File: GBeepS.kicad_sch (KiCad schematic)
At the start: 35 parts, among them J1 Ant, U1 NCP160xMX, U2 MMC3416xPJ, U3 ZOE-M8Q

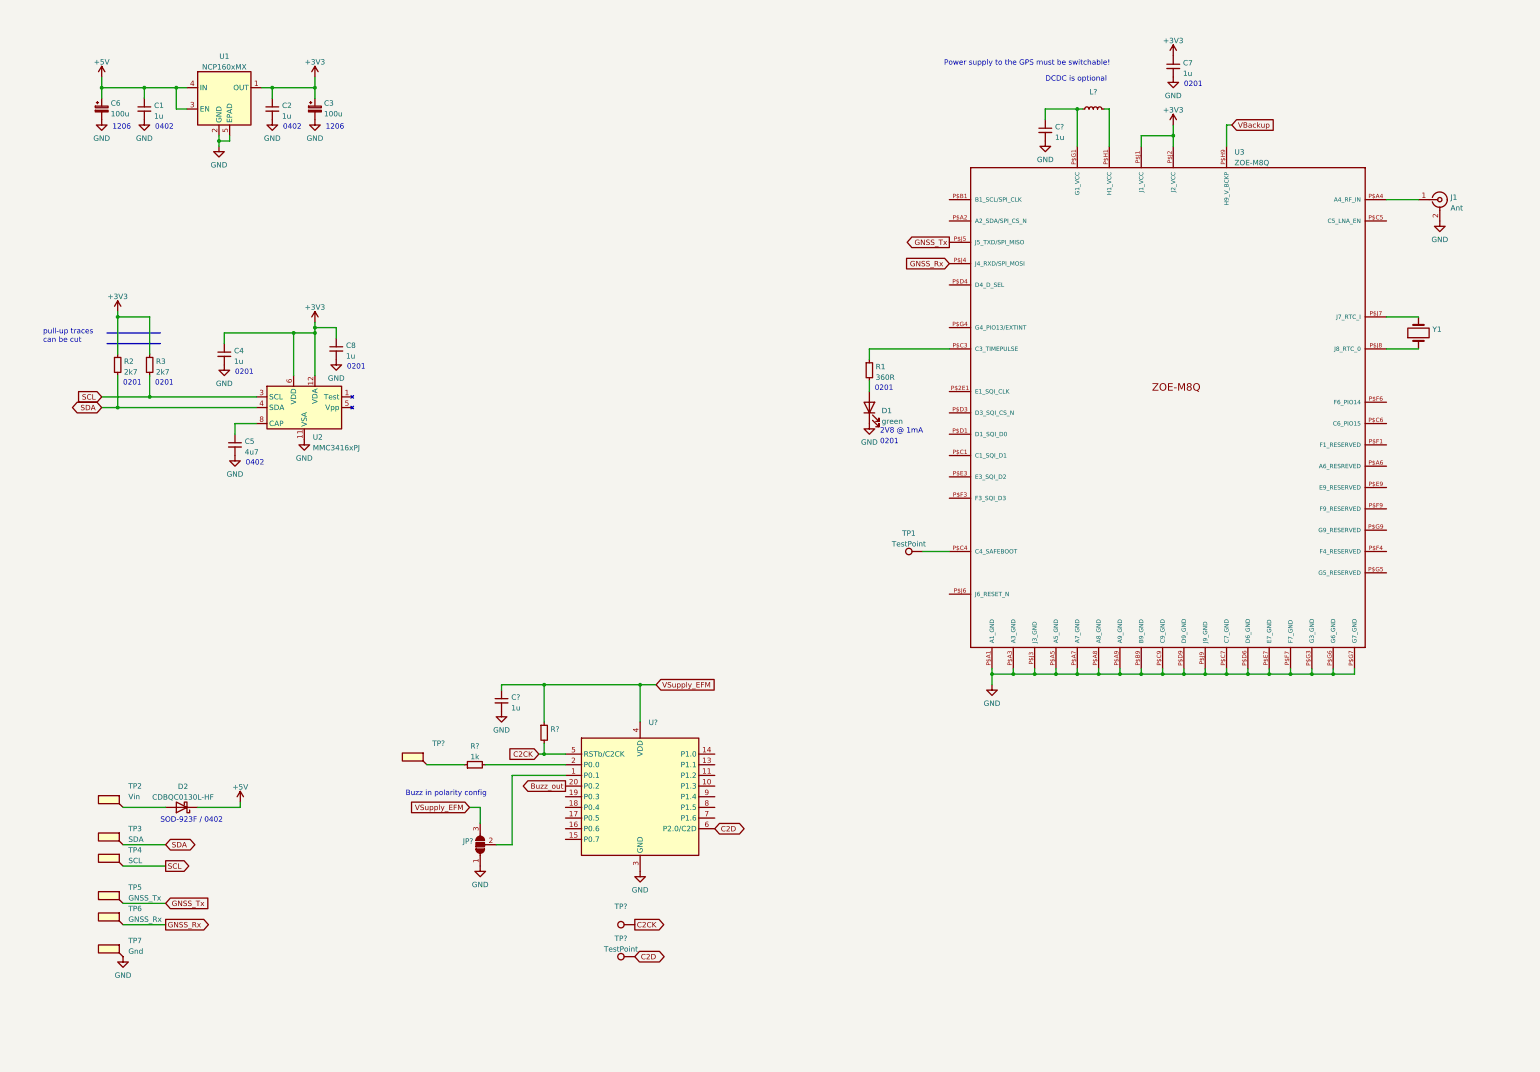
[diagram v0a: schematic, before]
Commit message: update schematic
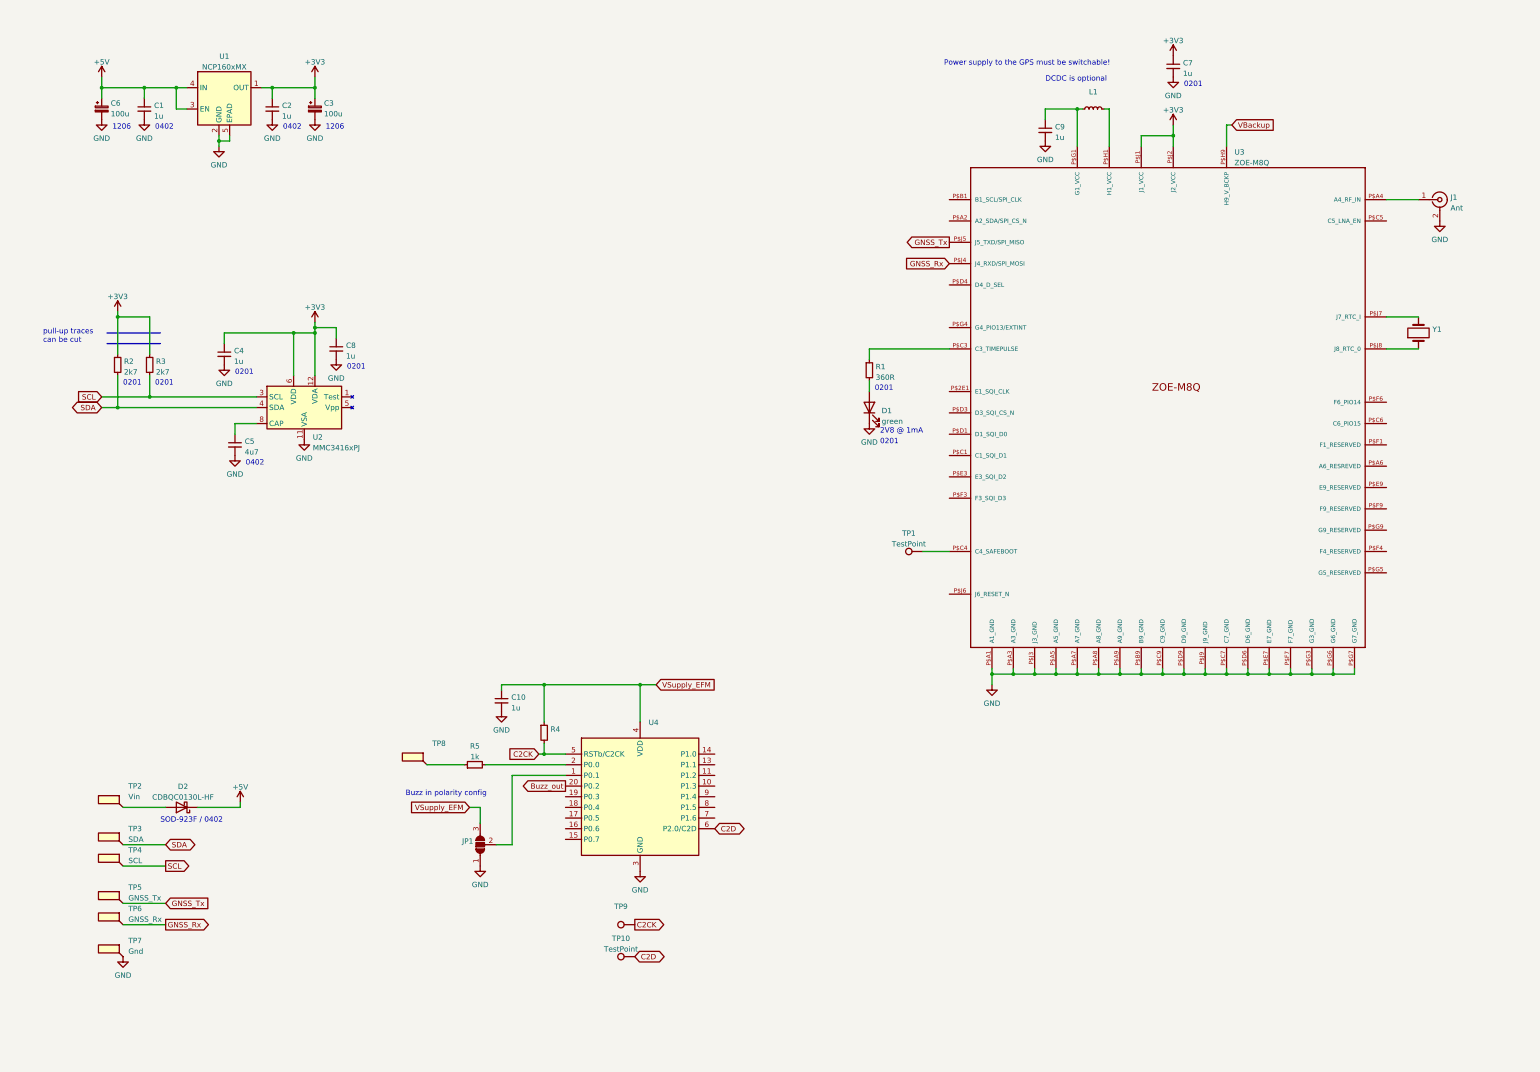
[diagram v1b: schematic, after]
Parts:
- gave numbers to parts that had none: 10
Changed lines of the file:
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@@
   (symbol (lib_id "MCU_SiliconLabs:EFM8BB10F8G-A-QFN20") (at 161.29 204.47 0) (unit 1)
     (in_bom yes) (on_board yes) (fields_autoplaced)
-    (property "Reference" "U?" (id 0) (at 163.3094 186.8002 0)
+    (property "Reference" "U4" (id 0) (at 163.3094 186.8002 0)
       (effects (font (size 1.27 1.27)) (justify left))
     )
@@
   (symbol (lib_id "Device:R_Small") (at 138.43 189.23 0) (unit 1)
     (in_bom yes) (on_board yes) (fields_autoplaced)
-    (property "Reference" "R?" (id 0) (at 139.9286 188.3953 0)
+    (property "Reference" "R4" (id 0) (at 139.9286 188.3953 0)
       (effects (font (size 1.27 1.27)) (justify left))
     )
@@
   (symbol (lib_id "Device:C_Small") (at 128.27 181.61 0) (unit 1)
     (in_bom yes) (on_board yes) (fields_autoplaced)
-    (property "Reference" "C?" (id 0) (at 130.5941 180.7816 0)
+    (property "Reference" "C10" (id 0) (at 130.5941 180.7816 0)
       (effects (font (size 1.27 1.27)) (justify left))
     )
@@
   (symbol (lib_id "Connector:TestPoint") (at 160.02 242.57 90) (unit 1)
     (in_bom yes) (on_board yes) (fields_autoplaced)
-    (property "Reference" "TP?" (id 0) (at 156.718 238.2352 90))
+    (property "Reference" "TP10" (id 0) (at 156.718 238.2352 90))
     (property "Value" "TestPoint" (id 1) (at 156.718 240.7721 90))
     (property "Footprint" "TestPoint:TestPoint_Pad_D1.0mm" (id 2) (at 160.02 237.49 0)
@@
   (symbol (lib_id "power:GND") (at 257.81 48.26 0) (unit 1)
     (in_bom yes) (on_board yes) (fields_autoplaced)
-    (property "Reference" "#PWR?" (id 0) (at 257.81 54.61 0)
+    (property "Reference" "#PWR0120" (id 0) (at 257.81 54.61 0)
       (effects (font (size 1.27 1.27)) hide)
     )
@@
   (symbol (lib_id "power:GND") (at 123.19 220.98 0) (unit 1)
     (in_bom yes) (on_board yes) (fields_autoplaced)
-    (property "Reference" "#PWR?" (id 0) (at 123.19 227.33 0)
+    (property "Reference" "#PWR0123" (id 0) (at 123.19 227.33 0)
       (effects (font (size 1.27 1.27)) hide)
     )
@@
   (symbol (lib_id "Device:R_Small") (at 121.92 196.85 90) (unit 1)
     (in_bom yes) (on_board yes) (fields_autoplaced)
-    (property "Reference" "R?" (id 0) (at 121.92 192.4136 90))
+    (property "Reference" "R5" (id 0) (at 121.92 192.4136 90))
     (property "Value" "1k" (id 1) (at 121.92 194.9505 90))
     (property "Footprint" "Yolo-GPS:R_0201_0603Metric_mod" (id 2) (at 121.92 196.85 0)
@@
   (symbol (lib_id "Device:C_Small") (at 257.81 45.72 0) (unit 1)
     (in_bom yes) (on_board yes) (fields_autoplaced)
-    (property "Reference" "C?" (id 0) (at 260.1341 44.8916 0)
+    (property "Reference" "C9" (id 0) (at 260.1341 44.8916 0)
       (effects (font (size 1.27 1.27)) (justify left))
     )
@@
   (symbol (lib_id "Device:L_Small") (at 269.24 40.64 90) (unit 1)
     (in_bom yes) (on_board yes) (fields_autoplaced)
-    (property "Reference" "L?" (id 0) (at 269.24 36.5592 90))
+    (property "Reference" "L1" (id 0) (at 269.24 36.5592 90))
     (property "Value" "" (id 1) (at 269.24 39.0961 90))
     (property "Footprint" "" (id 2) (at 269.24 40.64 0)
@@
   (symbol (lib_id "power:GND") (at 161.29 222.25 0) (unit 1)
     (in_bom yes) (on_board yes) (fields_autoplaced)
-    (property "Reference" "#PWR?" (id 0) (at 161.29 228.6 0)
+    (property "Reference" "#PWR0122" (id 0) (at 161.29 228.6 0)
       (effects (font (size 1.27 1.27)) hide)
     )
@@
   (symbol (lib_id "Connector:TestPoint_Flag") (at 110.49 196.85 0) (mirror y) (unit 1)
     (in_bom yes) (on_board yes)
-    (property "Reference" "TP?" (id 0) (at 111.76 191.7731 0)
+    (property "Reference" "TP8" (id 0) (at 111.76 191.7731 0)
       (effects (font (size 1.27 1.27)) (justify right))
     )
@@
   (symbol (lib_id "Connector:TestPoint") (at 160.02 234.95 90) (unit 1)
     (in_bom yes) (on_board yes) (fields_autoplaced)
-    (property "Reference" "TP?" (id 0) (at 156.718 230.6152 90))
+    (property "Reference" "TP9" (id 0) (at 156.718 230.6152 90))
     (property "Value" "" (id 1) (at 156.718 233.1521 90))
     (property "Footprint" "" (id 2) (at 160.02 229.87 0)
@@
   (symbol (lib_id "Jumper:SolderJumper_3_Open") (at 123.19 215.9 90) (unit 1)
     (in_bom yes) (on_board yes) (fields_autoplaced)
-    (property "Reference" "JP?" (id 0) (at 121.5391 215.0653 90)
+    (property "Reference" "JP1" (id 0) (at 121.5391 215.0653 90)
       (effects (font (size 1.27 1.27)) (justify left))
     )
@@
   (symbol (lib_id "power:GND") (at 128.27 184.15 0) (unit 1)
     (in_bom yes) (on_board yes) (fields_autoplaced)
-    (property "Reference" "#PWR?" (id 0) (at 128.27 190.5 0)
+    (property "Reference" "#PWR0121" (id 0) (at 128.27 190.5 0)
       (effects (font (size 1.27 1.27)) hide)
     )
@@
     )
     (path "/362bce95-f42a-4ba9-a3ee-b2ce531c8aa5"
-      (reference "#PWR?") (unit 1) (value "GND") (footprint "")
+      (reference "#PWR0120") (unit 1) (value "GND") (footprint "")
+    )
+    (path "/fc9ade7d-5b1e-48de-b80b-526521f39a61"
+      (reference "#PWR0121") (unit 1) (value "GND") (footprint "")
+    )
+    (path "/b6c5dab5-2177-4f56-9b1e-a65e67e58dc2"
+      (reference "#PWR0122") (unit 1) (value "GND") (footprint "")
     )
     (path "/5c3f7b5b-be71-4de8-a217-ecd631808e89"
-      (reference "#PWR?") (unit 1) (value "GND") (footprint "")
-    )
-    (path "/b6c5dab5-2177-4f56-9b1e-a65e67e58dc2"
-      (reference "#PWR?") (unit 1) (value "GND") (footprint "")
-    )
-    (path "/fc9ade7d-5b1e-48de-b80b-526521f39a61"
-      (reference "#PWR?") (unit 1) (value "GND") (footprint "")
+      (reference "#PWR0123") (unit 1) (value "GND") (footprint "")
     )
     (path "/7cdcb541-8b92-4799-8be1-cf2d204a844c"
@@
       (reference "C8") (unit 1) (value "1u") (footprint "Yolo-GPS:C_0201_0603Metric_mod")
     )
+    (path "/b0b0969f-60f9-48d0-9fb7-0fd9b1b264c0"
+      (reference "C9") (unit 1) (value "1u") (footprint "Yolo-GPS:C_0201_0603Metric_mod")
+    )
     (path "/0a828075-2672-4a17-82d1-67934faa18df"
-      (reference "C?") (unit 1) (value "1u") (footprint "Yolo-GPS:C_0201_0603Metric_mod")
-    )
-    (path "/b0b0969f-60f9-48d0-9fb7-0fd9b1b264c0"
-      (reference "C?") (unit 1) (value "1u") (footprint "Yolo-GPS:C_0201_0603Metric_mod")
+      (reference "C10") (unit 1) (value "1u") (footprint "Yolo-GPS:C_0201_0603Metric_mod")
     )
     (path "/ceb55e94-c665-4268-8d2a-eebc3d60110e"
@@
     )
     (path "/ea34cbf2-7287-4306-95bf-f7314f330629"
-      (reference "JP?") (unit 1) (value "SolderJumper_3_Open") (footprint "")
+      (reference "JP1") (unit 1) (value "SolderJumper_3_Open") (footprint "Jumper:SolderJumper-3_P1.3mm_Open_RoundedPad1.0x1.5mm")
     )
     (path "/b0b22e3b-ad5c-48af-acf9-0be147513efa"
-      (reference "L?") (unit 1) (value "L_Small") (footprint "")
+      (reference "L1") (unit 1) (value "L_Small") (footprint "Inductor_SMD:L_1008_2520Metric")
     )
     (path "/a58d788e-812d-4265-9ab4-13d606180491"
@@
     )
     (path "/05455e94-9ecd-49d5-b958-baf1bc2953e8"
-      (reference "R?") (unit 1) (value "1k") (footprint "Yolo-GPS:R_0201_0603Metric_mod")
+      (reference "R4") (unit 1) (value "1k") (footprint "Yolo-GPS:R_0201_0603Metric_mod")
     )
     (path "/a325107e-2244-480d-9a7b-a81602988eaa"
-      (reference "R?") (unit 1) (value "1k") (footprint "Yolo-GPS:R_0201_0603Metric_mod")
+      (reference "R5") (unit 1) (value "1k") (footprint "Yolo-GPS:R_0201_0603Metric_mod")
     )
     (path "/26f76493-c2ff-4ccd-b390-3b39bf4f9305"
@@
       (reference "TP7") (unit 1) (value "Gnd") (footprint "Yolo-GPS:pad_1x1.5")
     )
+    (path "/bd44b299-f41f-45ce-80f5-d42e57695646"
+      (reference "TP8") (unit 1) (value "Buzz_in") (footprint "Yolo-GPS:pad_1x1.5")
+    )
+    (path "/cc85315b-c2b5-4ab6-b04b-b25efceb1c6b"
+      (reference "TP9") (unit 1) (value "TestPoint") (footprint "TestPoint:TestPoint_Pad_D1.0mm")
+    )
     (path "/10865ba6-2c6e-457d-9fe4-5e9252b545e5"
-      (reference "TP?") (unit 1) (value "TestPoint") (footprint "TestPoint:TestPoint_Pad_D1.0mm")
-    )
-    (path "/bd44b299-f41f-45ce-80f5-d42e57695646"
-      (reference "TP?") (unit 1) (value "Buzz_in") (footprint "Yolo-GPS:pad_1x1.5")
-    )
-    (path "/cc85315b-c2b5-4ab6-b04b-b25efceb1c6b"
-      (reference "TP?") (unit 1) (value "TestPoint") (footprint "TestPoint:TestPoint_Pad_D1.0mm")
+      (reference "TP10") (unit 1) (value "TestPoint") (footprint "TestPoint:TestPoint_Pad_D1.0mm")
     )
     (path "/783ee3b3-a966-44bf-8463-a6b94b8c0e29"
@@
     )
     (path "/01bb07b7-5eda-4da8-b61b-2d6248635b61"
-      (reference "U?") (unit 1) (value "EFM8BB51F16G-A-QFN20") (footprint "Package_DFN_QFN:SiliconLabs_QFN-20-1EP_3x3mm_P0.5mm_EP1.8x1.8mm")
+      (reference "U4") (unit 1) (value "EFM8BB51F16G-A-QFN20") (footprint "Package_DFN_QFN:SiliconLabs_QFN-20-1EP_3x3mm_P0.5mm_EP1.8x1.8mm")
     )
     (path "/c7bd9338-9aed-41bb-820b-e4615e63ea41"
